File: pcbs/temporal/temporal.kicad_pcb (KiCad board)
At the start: 2 copper layers, 140.4 x 101.6 mm, 56 parts

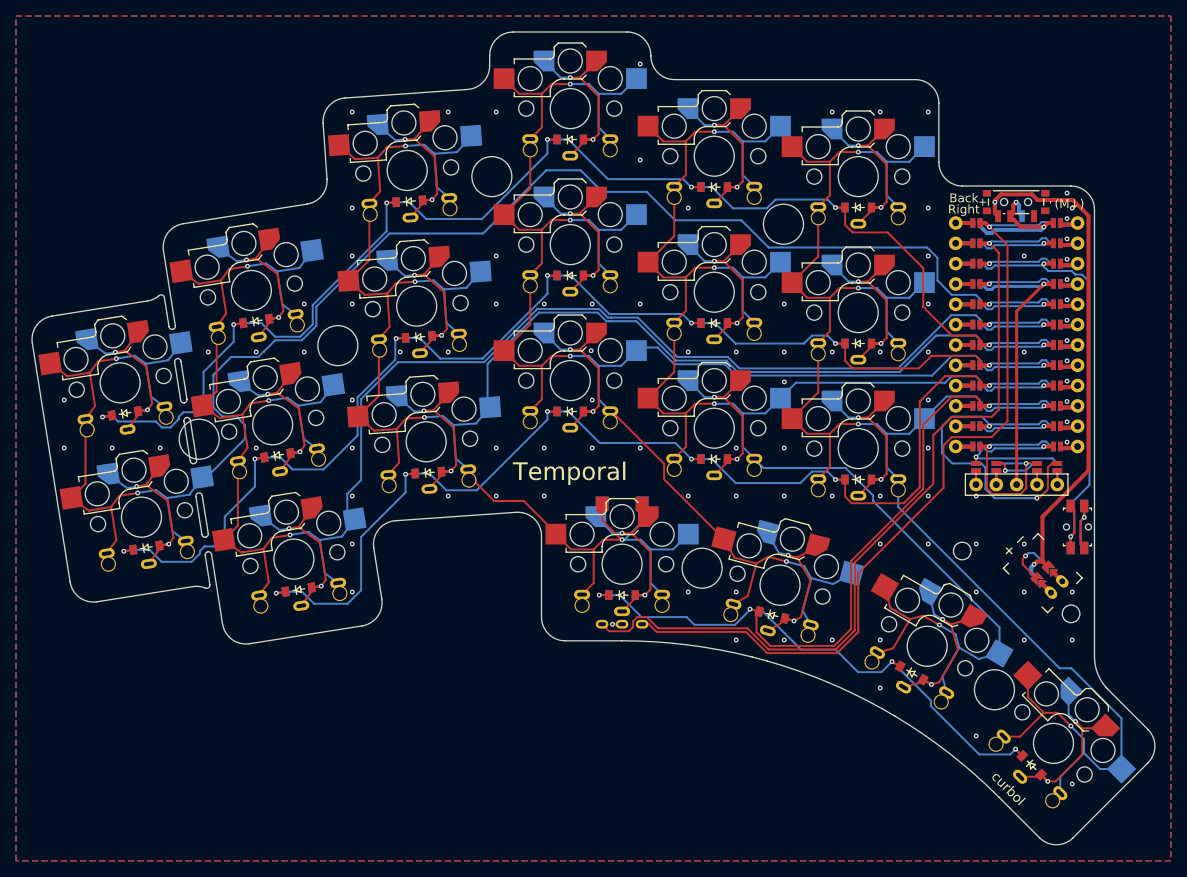
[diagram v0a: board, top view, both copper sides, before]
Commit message: Fold case STLs into per-variant folders and set silkscreen bold
Four strands, all verified together by make check.

Silkscreen is now bold. KiCad reaches a heavier Maple Mono only through the
bold attribute, since a weight-suffixed family name resolves to nothing, so
utility_text takes bold and mcu_nice_nano and power_switch_smd_side take
label_font_bold. Boards embed MapleMono-NF-Bold.ttf, and the text_thickness
warnings drop from 14 to 9 because the bold outlines carry more of the pen.

Case STLs are foldered rather than flat. Case keys now read in the order a
builder decides, temporal_<38|42>_<v1|v2>_<socket|solder>[_kickstand]_<hand>,
and convert_jscad.js maps that to cases/<count>/<generation>_<mounting>/. Two
choices land you in a directory holding only that variant's four files, instead
of scanning thirty-two names in one listing.

convert_jscad.js no longer converts its own leftovers. It writes <name>_hires
next to each input and unlinks it in a finally, but an interrupted run skips
that, and the input glob then picked the leftovers up as cases. One crash left
98 of them, so the following run built _hires_hires files and STLs under stale
names with _m_right unrenamed. The glob now ignores them.

pcbs/temporal was regenerated to pick up the bold silkscreen, and the hand
routing moved onto the new board: 354 traces and the six hand-added vias, on
the freshly stitched grid this time rather than the routed copy's. Thirty-four
segments then needed nudging by a median of 70 microns to clear stitching vias
the new grid had moved under them, four vias that genuinely shorted were
removed, and some pre-existing collinear stubs were cleaned up. 1209 segments
and 219 vias, DRC clean with nothing unconnected and no isolated copper.

The rest is comment cleanup across the scripts and the derived artifacts that
follow from all of the above.

Co-Authored-By: Claude Opus 5 (1M context) <noreply@anthropic.com>
Claude-Session: https://claude.ai/code/session_011XyDri8XNo1hSBhDE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
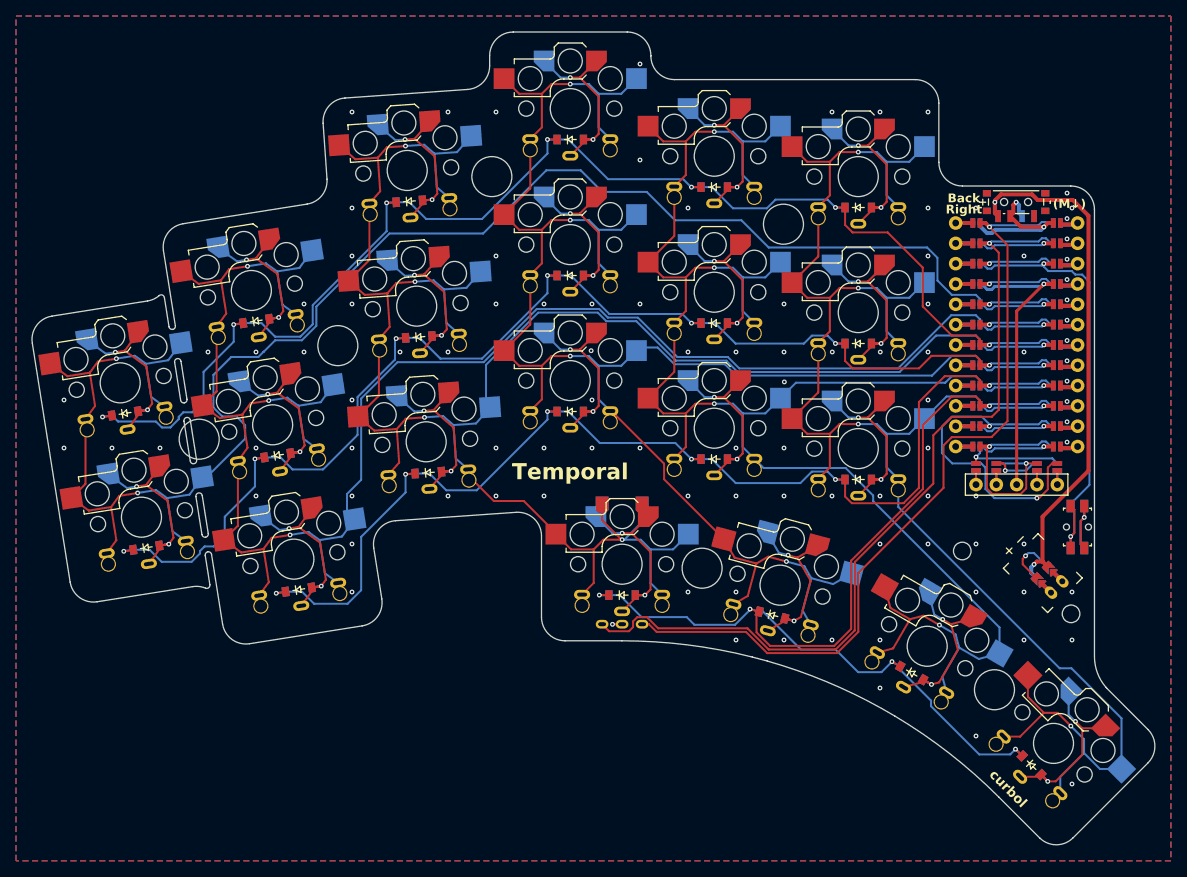
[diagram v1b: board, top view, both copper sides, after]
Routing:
- net GND: vias 105 -> 107
